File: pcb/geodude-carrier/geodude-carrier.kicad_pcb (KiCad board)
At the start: 2 copper layers, 177.3 x 152.3 mm, 44 parts, among them J1 12V, J2 12V, J3 GND, J30 SCL, J31 SCL, J32 SDA, J33 SDA, J34 3V3, J35 3V3, J36 5V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

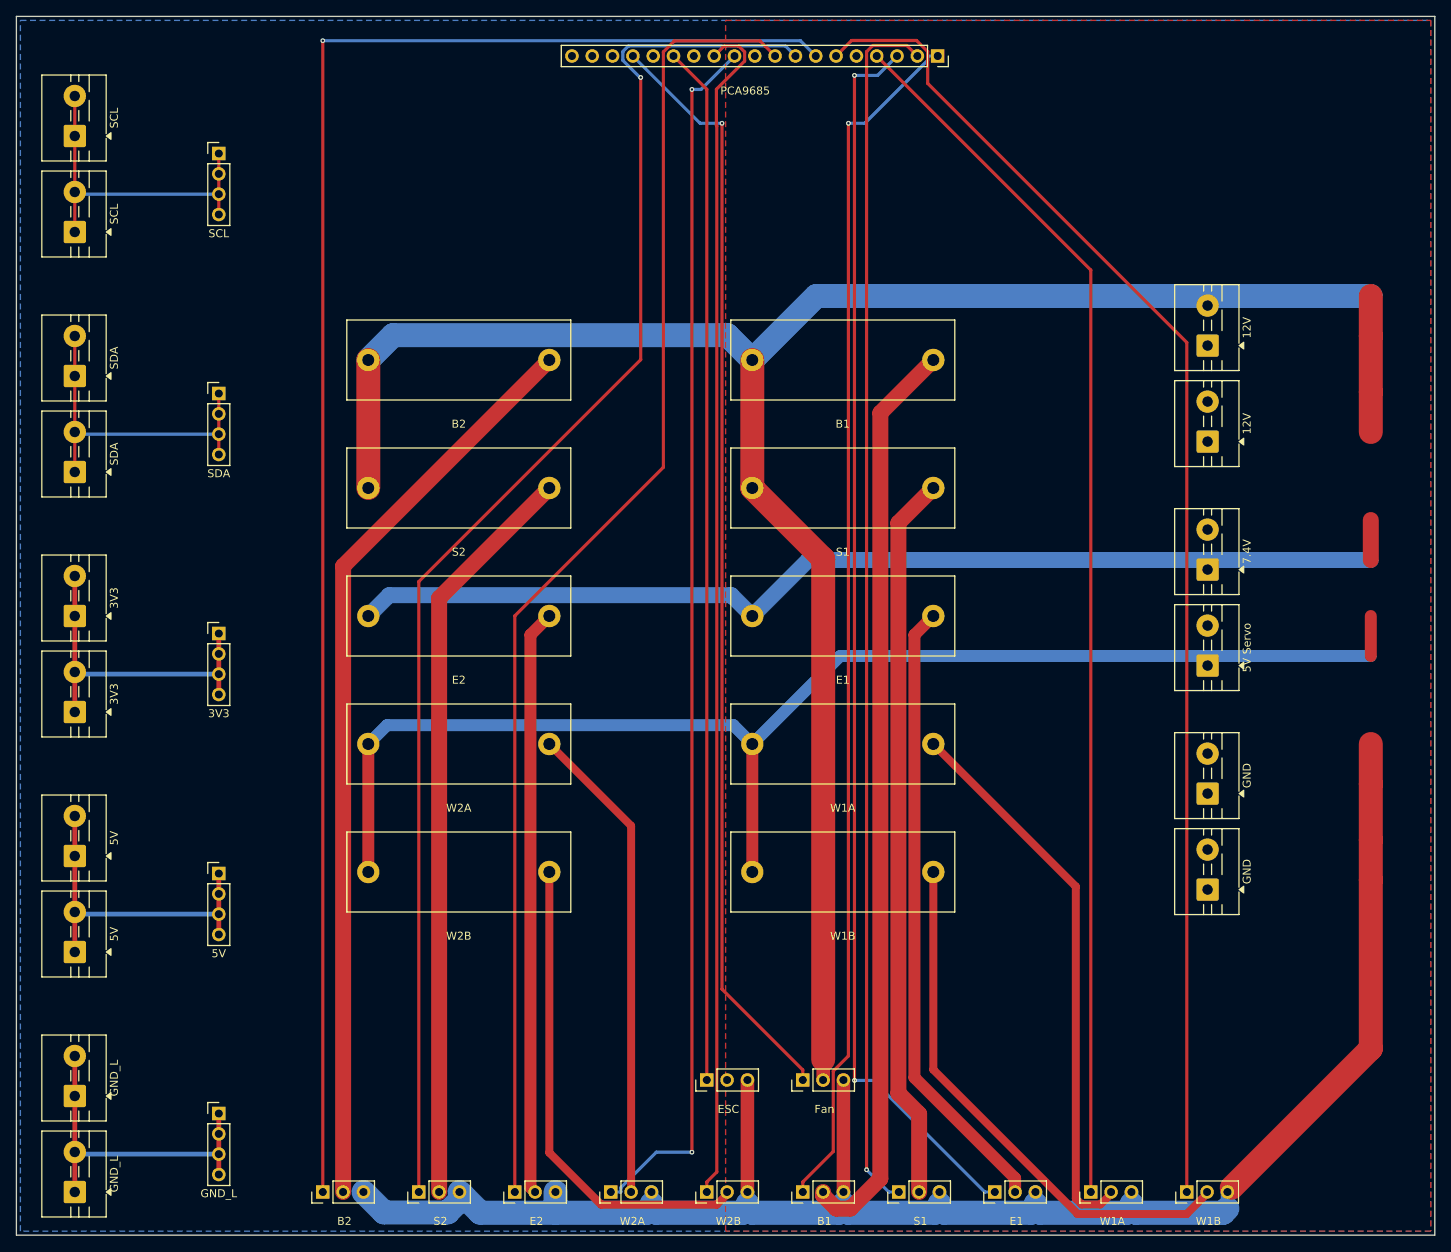
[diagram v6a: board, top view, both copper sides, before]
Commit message: Re-routed with updated placement, copper pours, Gerbers exported
233 tracks, 0 unconnected, 3 silk warnings, 1 thermal relief warning
GND pour B.Cu full board, +12V pour F.Cu right half
JLCPCB vias 0.3/0.4mm, Gerbers ready
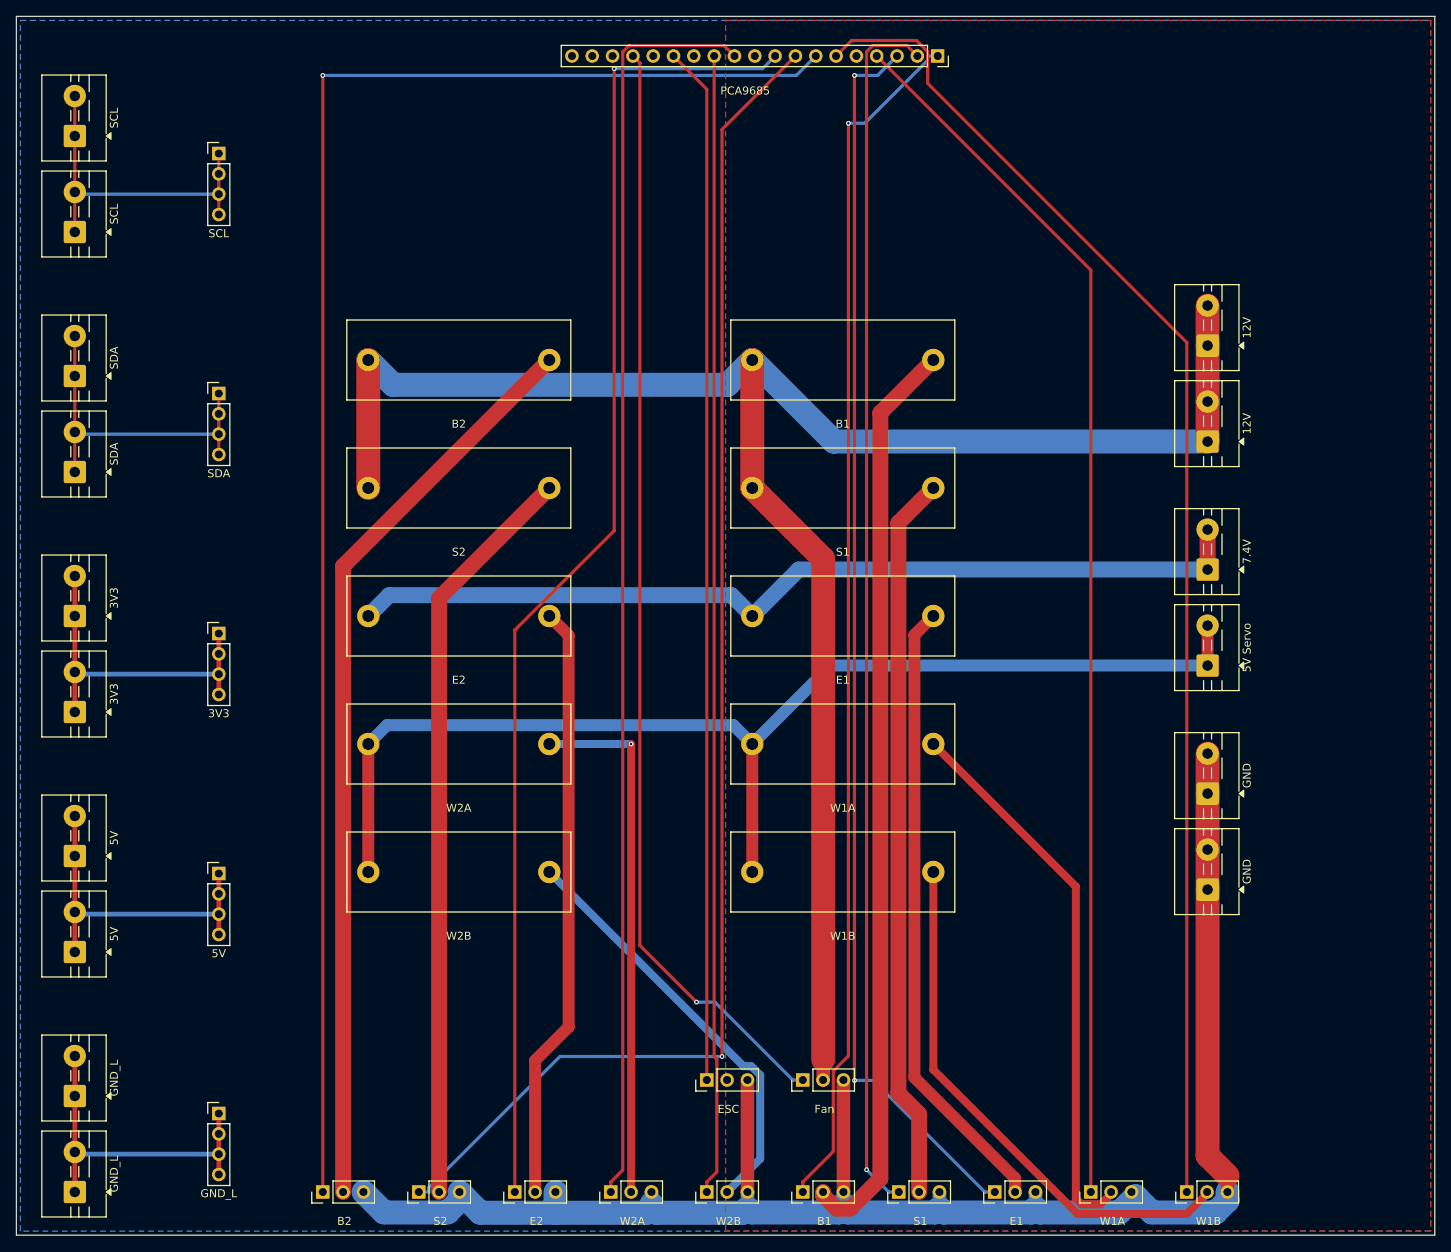
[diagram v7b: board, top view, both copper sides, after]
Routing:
- net +7V4: track 135.4 -> 114.5 mm
- net +5V_SERVO: track 168.8 -> 147.9 mm
- net +12V: track 257.9 -> 238.4 mm
- net GND: track 222.8 -> 214.5 mm
- net SV10_PWR: track 60.8 -> 53.2 mm
- net PWM_CH9: track 149.1 -> 142.7 mm
- net SV9_PWR: track 60.2 -> 66.2 mm, vias 0 -> 1
- net PWM_CH8: track 152.4 -> 158.0 mm, vias 2 -> 0
- net PWM_CH5: track 206.3 -> 202.2 mm
- net PWM_CH6: track 177.4 -> 174.1 mm
- net SV8_PWR: track 73.2 -> 74.7 mm
- net PWM_CH7: track 165.5 -> 166.3 mm, vias 0 -> 1

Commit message: Layout update
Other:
- board size 177.3 x 152.3 mm -> 155.3 x 152.3 mm
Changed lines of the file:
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@@
 	(gr_rect
 		(start 2.7 5.05)
-		(end 180 157.393796)
+		(end 158 157.393796)
 		(stroke
 			(width 0.1)
@@
 		(polygon
 			(pts
-				(xy 91.35 5.55) (xy 179.5 5.55) (xy 179.5 156.893796) (xy 91.35 156.893796)
+				(xy 91.35 5.55) (xy 158.6 5.55) (xy 158.6 156.893796) (xy 91.35 156.893796)
 			)
 		)
@@
 		(polygon
 			(pts
-				(xy 3.2 5.55) (xy 179.5 5.55) (xy 179.5 156.893796) (xy 3.2 156.893796)
+				(xy 3.2 5.55) (xy 158.4 5.55) (xy 158.4 156.893796) (xy 3.2 156.893796)
 			)
 		)
